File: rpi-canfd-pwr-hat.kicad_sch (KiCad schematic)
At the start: 81 parts, among them J1 Conn_01x02, J2 Conn_01x04_Pin, J3 Raspberry_Pi, J4 Conn_01x02, J5 Conn_01x02, U1 XC6206P332MR, U2 LM73100, U3 TPS259472A, U4 XC6206P182MR, U5 TPS56637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

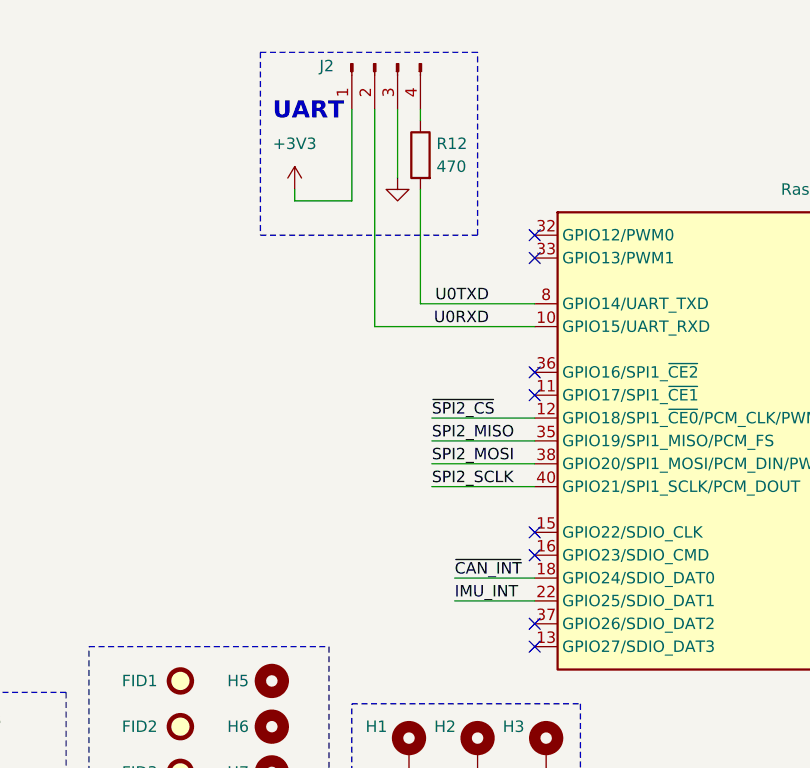
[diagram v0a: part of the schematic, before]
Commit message: pcb: route imu
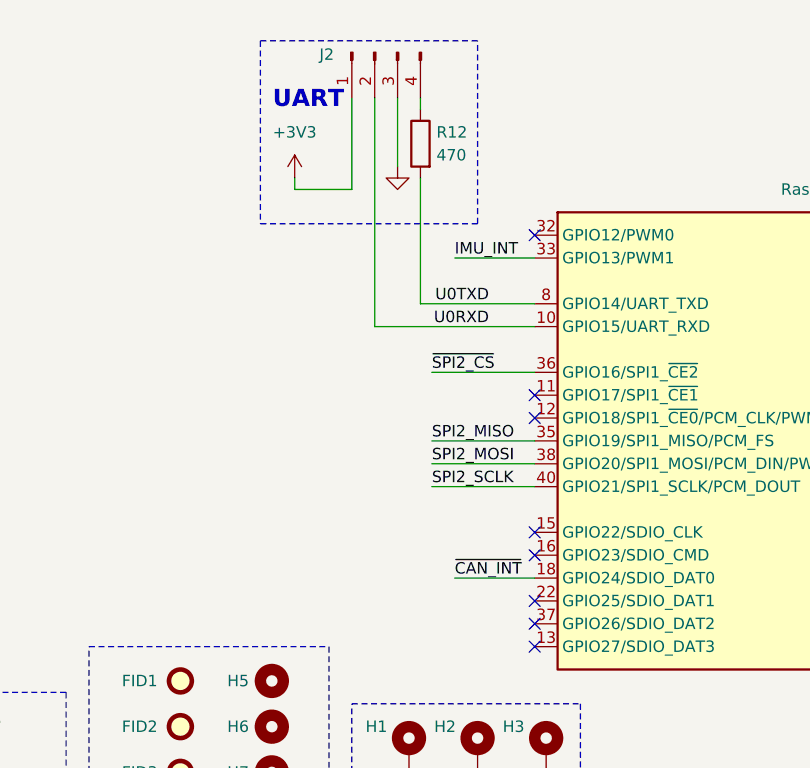
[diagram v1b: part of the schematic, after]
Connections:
- net IMU_INT: now also J3.33 (GPIO13/PWM1); no longer J3.22 (GPIO25/SDIO_DAT1)
- net ~{SPI2_CS}: now also J3.36 (GPIO16/SPI1_~{CE2}); no longer J3.12 (GPIO18/SPI1_~{CE0}/PCM_CLK/PWM0)
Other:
- moved on the sheet: J2, R12
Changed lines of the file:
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@@
 	)
 	(rectangle
-		(start 191.77 25.4)
-		(end 167.64 45.72)
+		(start 191.77 24.13)
+		(end 167.64 44.45)
 		(stroke
 			(width 0)
@@
 	(text "UART"
 		(exclude_from_sim no)
-		(at 172.974 32.004 0)
+		(at 172.974 30.734 0)
 		(effects
 			(font
@@
 	)
 	(no_connect
-		(at 198.12 48.26)
-	)
-	(no_connect
 		(at 264.16 73.66)
 	)
@@
 	)
 	(no_connect
+		(at 198.12 86.36)
+	)
+	(no_connect
 		(at 264.16 60.96)
 	)
@@
 	)
 	(no_connect
-		(at 198.12 60.96)
+		(at 198.12 66.04)
 	)
 	(no_connect
@@
 	(wire
 		(pts
-			(xy 185.42 33.02) (xy 185.42 31.75)
+			(xy 185.42 31.75) (xy 185.42 30.48)
 		)
 		(stroke
@@
 	(wire
 		(pts
+			(xy 189.23 48.26) (xy 198.12 48.26)
+		)
+		(stroke
+			(width 0)
+			(type default)
+		)
+	)
+	(wire
+		(pts
 			(xy 73.66 39.37) (xy 73.66 40.64)
 		)
@@
 	(wire
 		(pts
-			(xy 171.45 41.91) (xy 177.8 41.91)
+			(xy 171.45 40.64) (xy 177.8 40.64)
 		)
 		(stroke
@@
 	(wire
 		(pts
-			(xy 182.88 31.75) (xy 182.88 39.37)
+			(xy 182.88 30.48) (xy 182.88 38.1)
 		)
 		(stroke
@@
 	(wire
 		(pts
+			(xy 186.69 60.96) (xy 198.12 60.96)
+		)
+		(stroke
+			(width 0)
+			(type default)
+		)
+	)
+	(wire
+		(pts
 			(xy 167.64 158.75) (xy 167.64 160.02)
 		)
@@
 	(wire
 		(pts
-			(xy 171.45 40.64) (xy 171.45 41.91)
+			(xy 171.45 39.37) (xy 171.45 40.64)
 		)
 		(stroke
@@
 	(wire
 		(pts
-			(xy 189.23 86.36) (xy 198.12 86.36)
-		)
-		(stroke
-			(width 0)
-			(type default)
-		)
-	)
-	(wire
-		(pts
 			(xy 151.13 142.24) (xy 151.13 149.86)
 		)
@@
 	(wire
 		(pts
-			(xy 180.34 31.75) (xy 180.34 55.88)
+			(xy 180.34 30.48) (xy 180.34 55.88)
 		)
 		(stroke
@@
 	(wire
 		(pts
-			(xy 185.42 40.64) (xy 185.42 53.34)
+			(xy 185.42 39.37) (xy 185.42 53.34)
 		)
 		(stroke
@@
 	(wire
 		(pts
-			(xy 186.69 66.04) (xy 198.12 66.04)
-		)
-		(stroke
-			(width 0)
-			(type default)
-		)
-	)
-	(wire
-		(pts
 			(xy 138.43 104.14) (xy 137.16 104.14)
 		)
@@
 	(wire
 		(pts
-			(xy 177.8 41.91) (xy 177.8 31.75)
+			(xy 177.8 40.64) (xy 177.8 30.48)
 		)
 		(stroke
@@
 		)
 	)
+	(label "~{SPI2_CS}"
+		(at 186.69 60.96 0)
+		(effects
+			(font
+				(size 1.27 1.27)
+			)
+			(justify left bottom)
+		)
+	)
 	(label "SPI2_MISO"
 		(at 186.69 68.58 0)
@@
 		)
 	)
-	(label "~{SPI2_CS}"
-		(at 186.69 66.04 0)
-		(effects
-			(font
-				(size 1.27 1.27)
-			)
-			(justify left bottom)
-		)
-	)
 	(label "SPI2_MISO"
 		(at 130.81 78.74 180)
@@
 		)
 	)
-	(label "IMU_INT"
-		(at 189.23 86.36 0)
+	(label "SDA"
+		(at 165.1 180.34 180)
 		(effects
 			(font
 				(size 1.27 1.27)
 			)
-			(justify left bottom)
+			(justify right bottom)
 		)
 	)
-	(label "SDA"
-		(at 165.1 180.34 180)
+	(label "SPI_SCLK"
+		(at 165.1 137.16 0)
 		(effects
 			(font
 				(size 1.27 1.27)
 			)
-			(justify right bottom)
+			(justify left bottom)
 		)
 	)
-	(label "SPI_SCLK"
-		(at 165.1 137.16 0)
+	(label "IMU_INT"
+		(at 189.23 48.26 0)
 		(effects
 			(font
@@
 	(symbol
 		(lib_id "power:GND")
-		(at 182.88 39.37 0)
+		(at 182.88 38.1 0)
 		(mirror y)
 		(unit 1)
@@
 		(dnp no)
 		(property "Reference" "#PWR063"
-			(at 182.88 45.72 0)
+			(at 182.88 44.45 0)
 			(hide yes)
 			(show_name no)
@@
 		)
 		(property "Value" "GND"
-			(at 180.848 43.18 0)
+			(at 180.848 41.91 0)
 			(hide yes)
 			(show_name no)
@@
 		)
 		(property "Footprint" ""
-			(at 182.88 39.37 0)
+			(at 182.88 38.1 0)
 			(hide yes)
 			(show_name no)
@@
 		)
 		(property "Datasheet" ""
-			(at 182.88 39.37 0)
+			(at 182.88 38.1 0)
 			(hide yes)
 			(show_name no)
@@
 		)
 		(property "Description" "Power symbol creates a global label with name \"GND\" , ground"
-			(at 182.88 39.37 0)
+			(at 182.88 38.1 0)
 			(hide yes)
 			(show_name no)
@@
 	(symbol
 		(lib_id "power:+3V3")
-		(at 171.45 40.64 0)
+		(at 171.45 39.37 0)
 		(mirror y)
 		(unit 1)
@@
 		(fields_autoplaced yes)
 		(property "Reference" "#PWR062"
-			(at 171.45 44.45 0)
+			(at 171.45 43.18 0)
 			(hide yes)
 			(show_name no)
@@
 		)
 		(property "Value" "+3V3"
-			(at 171.45 35.56 0)
+			(at 171.45 34.29 0)
 			(show_name no)
 			(do_not_autoplace no)
@@
 		)
 		(property "Footprint" ""
-			(at 171.45 40.64 0)
+			(at 171.45 39.37 0)
 			(hide yes)
 			(show_name no)
@@
 		)
 		(property "Datasheet" ""
-			(at 171.45 40.64 0)
+			(at 171.45 39.37 0)
 			(hide yes)
 			(show_name no)
@@
 		)
 		(property "Description" "Power symbol creates a global label with name \"+3V3\""
-			(at 171.45 40.64 0)
+			(at 171.45 39.37 0)
 			(hide yes)
 			(show_name no)
@@
 	(symbol
 		(lib_id "Device:R")
-		(at 185.42 36.83 0)
+		(at 185.42 35.56 0)
 		(mirror y)
 		(unit 1)
@@
 		(dnp no)
 		(property "Reference" "R12"
-			(at 187.198 35.56 0)
+			(at 187.198 34.29 0)
 			(show_name no)
 			(do_not_autoplace no)
@@
 		)
 		(property "Value" "470"
-			(at 187.198 38.1 0)
+			(at 187.198 36.83 0)
 			(show_name no)
 			(do_not_autoplace no)
@@
 		)
 		(property "Footprint" "Resistor_SMD:R_0402_1005Metric"
-			(at 187.198 36.83 90)
+			(at 187.198 35.56 90)
 			(hide yes)
 			(show_name no)
@@
 		)
 		(property "Datasheet" ""
-			(at 185.42 36.83 0)
+			(at 185.42 35.56 0)
 			(hide yes)
 			(show_name no)
@@
 		)
 		(property "Description" "Resistor"
-			(at 185.42 36.83 0)
+			(at 185.42 35.56 0)
 			(hide yes)
 			(show_name no)
@@
 		)
 		(property "Basic" "Y"
-			(at 185.42 36.83 0)
+			(at 185.42 35.56 0)
 			(hide yes)
 			(show_name no)
@@
 		)
 		(property "JLCPCB Part #" "C25117"
-			(at 185.42 36.83 0)
+			(at 185.42 35.56 0)
 			(hide yes)
 			(show_name no)
@@
 		)
 		(property "Manufacturer" "Uniroyal Elec"
-			(at 185.42 36.83 0)
+			(at 185.42 35.56 0)
 			(hide yes)
 			(show_name no)
@@
 		)
 		(property "Manufacturer Part Number" "0402WGF4700TCE"
-			(at 185.42 36.83 0)
+			(at 185.42 35.56 0)
 			(hide yes)
 			(show_name no)
@@
 	(symbol
 		(lib_id "Connector:Conn_01x04_Pin")
-		(at 180.34 26.67 90)
+		(at 180.34 25.4 90)
 		(mirror x)
 		(unit 1)
@@
 		(dnp no)
 		(property "Reference" "J2"
-			(at 175.006 26.924 90)
+			(at 175.006 25.654 90)
 			(show_name no)
 			(do_not_autoplace no)
@@
 		)
 		(property "Value" "Conn_01x04_Pin"
-			(at 181.61 24.13 90)
+			(at 181.61 22.86 90)
 			(hide yes)
 			(show_name no)
@@
 		)
 		(property "Footprint" "Connector_PinHeader_2.54mm:PinHeader_1x04_P2.54mm_Vertical"
-			(at 180.34 26.67 0)
+			(at 180.34 25.4 0)
 			(hide yes)
 			(show_name no)
@@
 		)
 		(property "Datasheet" ""
-			(at 180.34 26.67 0)
+			(at 180.34 25.4 0)
 			(hide yes)
 			(show_name no)
@@
 		)
 		(property "Description" "Generic connector, single row, 01x04, script generated"
-			(at 180.34 26.67 0)
+			(at 180.34 25.4 0)
 			(hide yes)
 			(show_name no)

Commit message: pcb: route can
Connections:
- net ~{CAN_INT}: now also J3.26 (~{CE1}_SPI0/GPIO07); no longer J3.18 (GPIO24/SDIO_DAT0)
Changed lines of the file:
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@@
 	)
 	(no_connect
-		(at 264.16 78.74)
-	)
-	(no_connect
 		(at 198.12 86.36)
 	)
@@
 	)
 	(no_connect
+		(at 198.12 83.82)
+	)
+	(no_connect
 		(at 198.12 91.44)
 	)
@@
 	(wire
 		(pts
-			(xy 58.42 60.96) (xy 59.69 60.96)
+			(xy 274.32 78.74) (xy 264.16 78.74)
 		)
 		(stroke
@@
 	(wire
 		(pts
-			(xy 73.66 71.12) (xy 68.58 71.12)
+			(xy 58.42 60.96) (xy 59.69 60.96)
 		)
 		(stroke
@@
 	(wire
 		(pts
-			(xy 167.64 149.86) (xy 173.99 149.86)
+			(xy 73.66 71.12) (xy 68.58 71.12)
 		)
 		(stroke
@@
 	(wire
 		(pts
-			(xy 151.13 190.5) (xy 151.13 191.77)
+			(xy 167.64 149.86) (xy 173.99 149.86)
 		)
 		(stroke
@@
 	(wire
 		(pts
-			(xy 40.64 39.37) (xy 40.64 40.64)
+			(xy 151.13 190.5) (xy 151.13 191.77)
 		)
 		(stroke
@@
 	(wire
 		(pts
-			(xy 189.23 83.82) (xy 198.12 83.82)
+			(xy 40.64 39.37) (xy 40.64 40.64)
 		)
 		(stroke
@@
 		)
 	)
+	(label "~{CAN_INT}"
+		(at 274.32 78.74 180)
+		(effects
+			(font
+				(size 1.27 1.27)
+			)
+			(justify right bottom)
+		)
+	)
 	(label "SPI2_MISO_1V8"
 		(at 96.52 116.84 0)
@@
 		)
 	)
-	(label "~{CAN_INT}"
-		(at 189.23 83.82 0)
-		(effects
-			(font
-				(size 1.27 1.27)
-			)
-			(justify left bottom)
-		)
-	)

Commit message: generate production files
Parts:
- U9: JLCPCB Part # C22433320 -> C30111221; Manufacturer Part Number TCAN3413DR -> TCAN3413DDFR
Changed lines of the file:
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@@
 			)
 		)
-		(property "JLCPCB Part #" "C22433320"
+		(property "JLCPCB Part #" "C30111221"
 			(at 243.84 134.62 0)
 			(hide yes)
@@
 			)
 		)
-		(property "Manufacturer Part Number" "TCAN3413DR"
+		(property "Manufacturer Part Number" "TCAN3413DDFR"
 			(at 243.84 134.62 0)
 			(hide yes)

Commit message: schem/pcb: switch to phat rubycon cap
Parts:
- C16: footprint Capacitor_SMD:CP_Elec_6.3x7.7 -> Capacitor_SMD:CP_Elec_10x10.5; JLCPCB Part # C2918361 -> C88818; Manufacturer ROQANG -> Rubycon; Manufacturer Part Number RVT1E221M0607 -> 50TZV220M10X10.5
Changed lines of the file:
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@@
 			)
 		)
-		(property "Footprint" "Capacitor_SMD:CP_Elec_6.3x7.7"
+		(property "Footprint" "Capacitor_SMD:CP_Elec_10x10.5"
 			(at 82.8548 116.84 0)
 			(hide yes)
@@
 			)
 		)
-		(property "JLCPCB Part #" "C2918361"
+		(property "JLCPCB Part #" "C88818"
 			(at 83.82 113.03 0)
 			(hide yes)
@@
 			)
 		)
-		(property "Manufacturer" "ROQANG"
+		(property "Manufacturer" "Rubycon"
 			(at 83.82 113.03 0)
 			(hide yes)
@@
 			)
 		)
-		(property "Manufacturer Part Number" "RVT1E221M0607"
+		(property "Manufacturer Part Number" "50TZV220M10X10.5"
 			(at 83.82 113.03 0)
 			(hide yes)
